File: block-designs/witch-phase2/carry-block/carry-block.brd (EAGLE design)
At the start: 27.9 x 27.9 mm, 11 parts, among them IC1 741G175, IC2 74AHC1G32DBV, IC3 74LS195D, IC4 74AHC1G86DBV

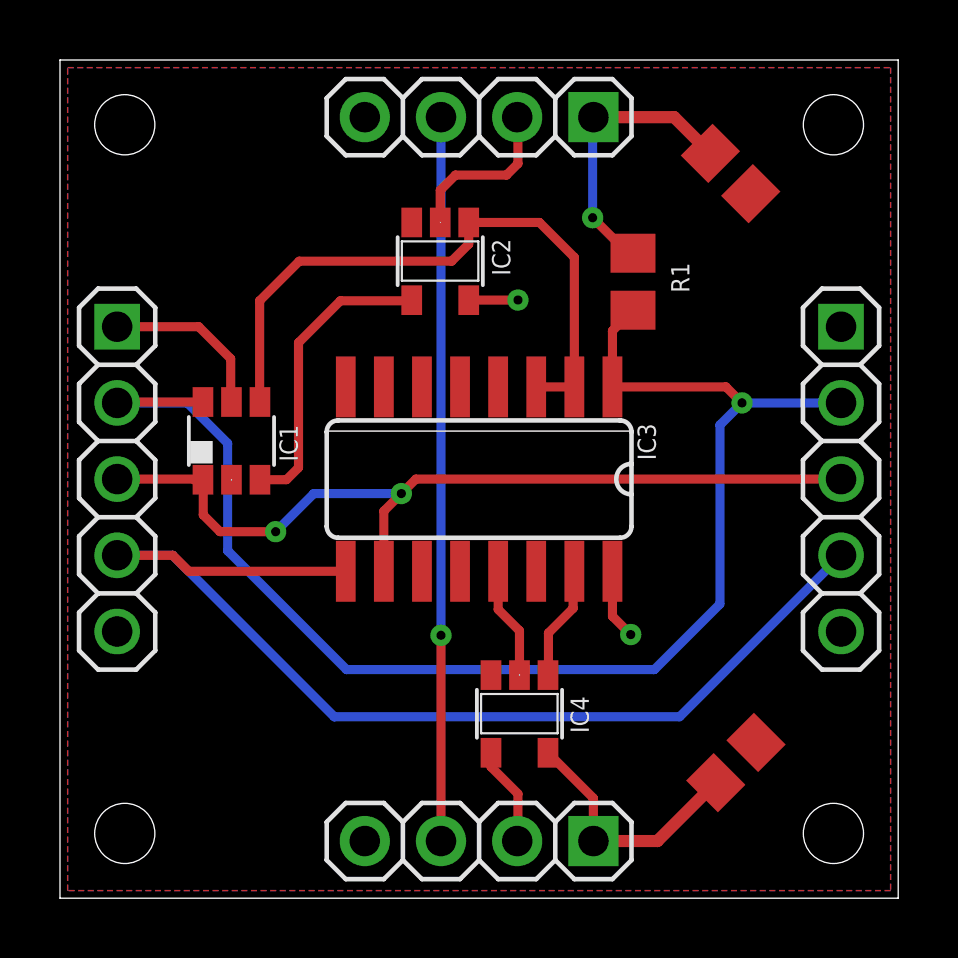
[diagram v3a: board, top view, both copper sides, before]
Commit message: replace or with d-flipflop to fix zc start issue
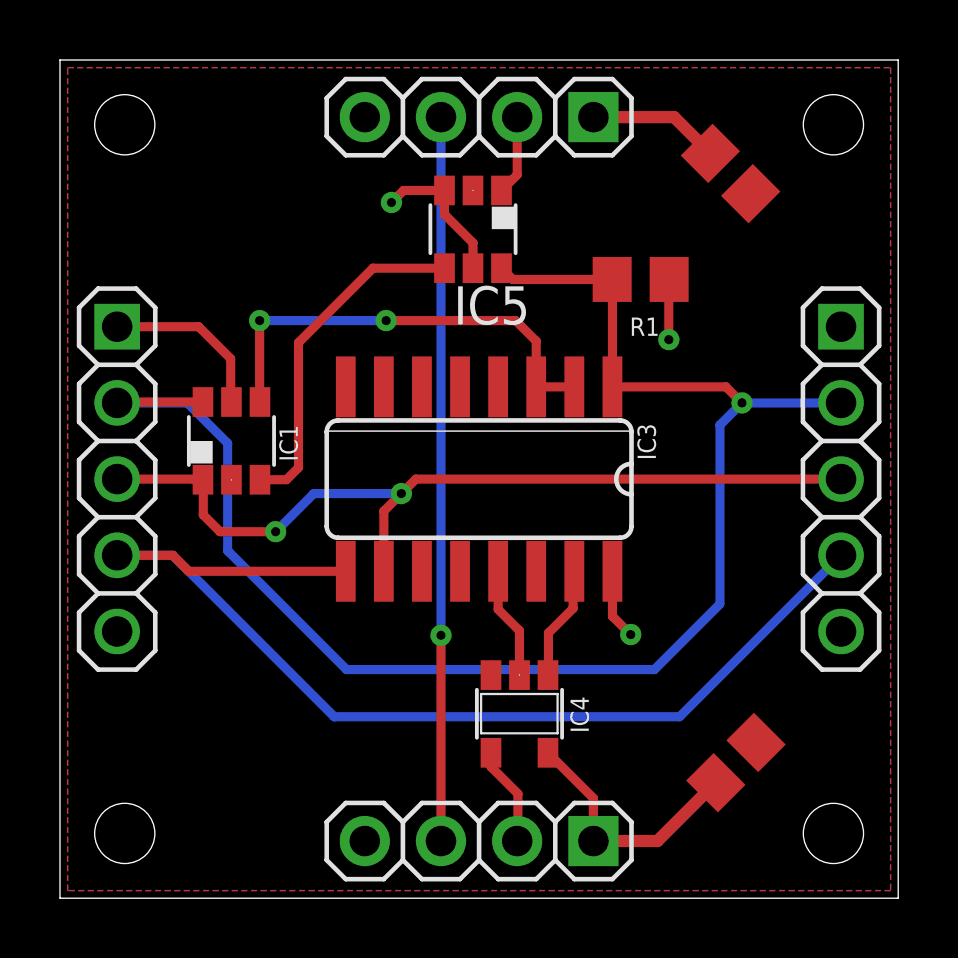
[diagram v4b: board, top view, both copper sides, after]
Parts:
- removed IC2: 74AHC1G32DBV, 74xx-little-us:SOT23-5
- added IC5: 741G175, 74xx-little-us:DBV_R-PDSO-G6
- moved R1 0.27 mm to (19.4, 20.6), turned to 180 degrees
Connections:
- net !RST: now also IC5.6
- net GND: now also IC5.2; no longer IC2.3
- net N$5: now also IC5.4; no longer IC2.4
- net VCC: now also IC5.3, IC5.5; no longer IC2.5
- net ZC: now also IC5.1; no longer IC2.2
- net ZC-OUT: no longer IC2.1
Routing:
- net ZC-OUT: track 21.5 -> 15.1 mm, vias 0 -> 2
- net !RST: track 47.3 -> 51.9 mm
- net ZC: track 5.59 -> 2.66 mm
- net N$5: track 9.98 -> 11.5 mm
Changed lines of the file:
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@@
 <?xml version="1.0" encoding="utf-8"?>
 <!DOCTYPE eagle SYSTEM "eagle.dtd">
-<eagle version="7.3.0">
+<eagle version="7.6.0">
 <drawing>
 <settings>
@@
 <attribute name="VALUE" x="22.86" y="17.78" size="1.27" layer="27" rot="R270"/>
 </element>
-<element name="IC2" library="74xx-little-us" package="SOT23-5" value="74AHC1G32DBV" x="12.6746" y="21.2344" smashed="yes" rot="R180">
-<attribute name="NAME" x="15.0114" y="20.7518" size="0.6096" layer="25" rot="R90"/>
-<attribute name="VALUE" x="15.9766" y="21.5646" size="0.6096" layer="27" rot="R180"/>
-</element>
-<element name="R1" library="resistor" package="R0805" value="" x="19.1008" y="20.5486" smashed="yes" rot="R270">
-<attribute name="NAME" x="20.3708" y="21.1836" size="0.6096" layer="25" rot="R270"/>
-<attribute name="VALUE" x="16.5608" y="21.1836" size="1.27" layer="27" rot="R270"/>
+<element name="R1" library="resistor" package="R0805" value="" x="19.3548" y="20.6248" smashed="yes" rot="R180">
+<attribute name="NAME" x="19.9898" y="19.3548" size="0.6096" layer="25" rot="R180"/>
+<attribute name="VALUE" x="19.9898" y="23.1648" size="1.27" layer="27" rot="R180"/>
 </element>
 <element name="IC1" library="74xx-little-us" package="DBV_R-PDSO-G6" value="741G175" x="5.715" y="15.24" smashed="yes">
@@
 <attribute name="NAME" x="19.2532" y="15.8242" size="0.6096" layer="25" ratio="10" rot="R270"/>
 </element>
+<element name="IC5" library="74xx-little-us" package="DBV_R-PDSO-G6" value="741G175" x="13.7668" y="22.3012" rot="R180"/>
 </elements>
 <signals>
@@
 <vertex x="27.686" y="27.686"/>
 </polygon>
-<contactref element="IC2" pad="3"/>
 <contactref element="IC1" pad="2"/>
 <contactref element="JP2" pad="5"/>
@@
 <contactref element="IC3" pad="5"/>
 <contactref element="IC3" pad="6"/>
+<contactref element="IC5" pad="2"/>
 </signal>
 <signal name="VCC">
@@
 <contactref element="JP4" pad="1"/>
 <contactref element="JP2" pad="1"/>
-<contactref element="IC2" pad="5"/>
 <contactref element="R1" pad="1"/>
 <contactref element="IC1" pad="5"/>
@@
 <wire x1="16.2662" y1="4.8468" x2="17.78" y2="3.333" width="0.3048" layer="1"/>
 <wire x1="17.78" y1="3.333" x2="17.78" y2="1.905" width="0.3048" layer="1"/>
-<wire x1="13.6246" y1="19.9344" x2="13.6292" y2="19.939" width="0.3048" layer="1"/>
-<wire x1="13.6292" y1="19.939" x2="15.2654" y2="19.939" width="0.3048" layer="1"/>
-<via x="15.2654" y="19.939" extent="1-16" drill="0.3048"/>
+<via x="11.049" y="23.1902" extent="1-16" drill="0.3048"/>
 <wire x1="4.6228" y1="19.05" x2="5.6896" y2="17.9832" width="0.3048" layer="1"/>
 <wire x1="5.6896" y1="17.9832" x2="5.6896" y2="16.5654" width="0.3048" layer="1"/>
 <wire x1="5.6896" y1="16.5654" x2="5.715" y2="16.54" width="0.3048" layer="1"/>
-<wire x1="19.1008" y1="21.4986" x2="18.9382" y2="21.4986" width="0.3048" layer="1"/>
-<wire x1="18.9382" y1="21.4986" x2="17.7546" y2="22.6822" width="0.3048" layer="1"/>
-<via x="17.7546" y="22.6822" extent="1-16" drill="0.3048"/>
-<wire x1="17.7546" y1="22.6822" x2="17.7546" y2="26.0096" width="0.3048" layer="16"/>
+<via x="20.2946" y="18.6182" extent="1-16" drill="0.3048"/>
 <wire x1="17.7546" y1="26.0096" x2="17.78" y2="26.035" width="0.3048" layer="16"/>
 <wire x1="17.78" y1="26.035" x2="20.472396875" y2="26.035" width="0.4064" layer="1"/>
@@
 <wire x1="21.858046875" y1="3.849446875" x2="19.9136" y2="1.905" width="0.4064" layer="1"/>
 <wire x1="19.9136" y1="1.905" x2="17.78" y2="1.905" width="0.4064" layer="1"/>
+<contactref element="IC5" pad="5"/>
+<contactref element="IC5" pad="3"/>
+<wire x1="20.3048" y1="20.6248" x2="20.2946" y2="20.6146" width="0.3048" layer="1"/>
+<wire x1="20.2946" y1="20.6146" x2="20.2946" y2="18.6182" width="0.3048" layer="1"/>
+<wire x1="12.8168" y1="23.5912" x2="11.45" y2="23.5912" width="0.3048" layer="1"/>
+<wire x1="11.45" y1="23.5912" x2="11.049" y2="23.1902" width="0.3048" layer="1"/>
+<wire x1="12.8168" y1="23.5912" x2="12.8168" y2="22.794" width="0.3048" layer="1"/>
+<wire x1="12.8168" y1="22.794" x2="13.7668" y2="21.844" width="0.3048" layer="1"/>
+<wire x1="13.7668" y1="21.844" x2="13.7668" y2="21.0012" width="0.3048" layer="1"/>
 </signal>
 <signal name="ZC">
 <contactref element="JP1" pad="2"/>
-<contactref element="IC2" pad="2"/>
-<wire x1="12.6746" y1="22.5244" x2="12.6746" y2="23.5966" width="0.3048" layer="1"/>
-<wire x1="12.6746" y1="23.5966" x2="13.1826" y2="24.1046" width="0.3048" layer="1"/>
-<wire x1="13.1826" y1="24.1046" x2="14.8844" y2="24.1046" width="0.3048" layer="1"/>
-<wire x1="14.8844" y1="24.1046" x2="15.2654" y2="24.4856" width="0.3048" layer="1"/>
-<wire x1="15.2654" y1="24.4856" x2="15.2654" y2="26.0096" width="0.3048" layer="1"/>
-<wire x1="15.2654" y1="26.0096" x2="15.24" y2="26.035" width="0.3048" layer="1"/>
+<contactref element="IC5" pad="1"/>
+<wire x1="14.7168" y1="23.5912" x2="15.24" y2="24.1144" width="0.3048" layer="1"/>
+<wire x1="15.24" y1="24.1144" x2="15.24" y2="26.035" width="0.3048" layer="1"/>
 </signal>
 <signal name="CLK_OUT">
@@
 </signal>
 <signal name="ZC-OUT">
-<contactref element="IC2" pad="1"/>
 <contactref element="IC1" pad="4"/>
 <contactref element="IC3" pad="3"/>
@@
 <wire x1="15.875" y1="17.0434" x2="17.145" y2="17.0434" width="0.3048" layer="1"/>
 <wire x1="17.1196" y1="17.0688" x2="17.145" y2="17.0434" width="0.3048" layer="1"/>
-<wire x1="13.6398" y1="22.5396" x2="13.6246" y2="22.5244" width="0.3048" layer="1"/>
-<wire x1="13.6246" y1="22.5244" x2="15.982" y2="22.5244" width="0.3048" layer="1"/>
-<wire x1="15.982" y1="22.5244" x2="17.145" y2="21.3614" width="0.3048" layer="1"/>
-<wire x1="17.145" y1="21.3614" x2="17.145" y2="17.0434" width="0.3048" layer="1"/>
-<wire x1="13.0556" y1="21.2344" x2="13.6246" y2="21.8034" width="0.3048" layer="1"/>
-<wire x1="13.6246" y1="21.8034" x2="13.6246" y2="22.5244" width="0.3048" layer="1"/>
-<wire x1="13.0556" y1="21.2344" x2="7.9756" y2="21.2344" width="0.3048" layer="1"/>
-<wire x1="7.9756" y1="21.2344" x2="6.6548" y2="19.9136" width="0.3048" layer="1"/>
-<wire x1="6.6548" y1="19.9136" x2="6.6548" y2="16.5502" width="0.3048" layer="1"/>
 <wire x1="6.6548" y1="16.5502" x2="6.665" y2="16.54" width="0.3048" layer="1"/>
+<via x="6.6548" y="19.2532" extent="1-16" drill="0.3048"/>
+<wire x1="6.6548" y1="19.2532" x2="10.8712" y2="19.2532" width="0.3048" layer="16"/>
+<via x="10.8712" y="19.2532" extent="1-16" drill="0.3048"/>
+<wire x1="10.8712" y1="19.2532" x2="15.1892" y2="19.2532" width="0.3048" layer="1"/>
+<wire x1="15.1892" y1="19.2532" x2="15.875" y2="18.5674" width="0.3048" layer="1"/>
+<wire x1="15.875" y1="18.5674" x2="15.875" y2="17.0434" width="0.3048" layer="1"/>
+<wire x1="6.6548" y1="16.5502" x2="6.6548" y2="19.2532" width="0.3048" layer="1"/>
 </signal>
 <signal name="N$5">
-<contactref element="IC2" pad="4"/>
 <contactref element="IC1" pad="3"/>
 <wire x1="7.9502" y1="14.351" x2="7.5492" y2="13.95" width="0.3048" layer="1"/>
 <wire x1="7.9502" y1="14.351" x2="7.9502" y2="18.5166" width="0.3048" layer="1"/>
-<wire x1="7.9502" y1="18.5166" x2="9.3472" y2="19.9136" width="0.3048" layer="1"/>
-<wire x1="9.3472" y1="19.9136" x2="11.7038" y2="19.9136" width="0.3048" layer="1"/>
-<wire x1="11.7038" y1="19.9136" x2="11.7246" y2="19.9344" width="0.3048" layer="1"/>
 <wire x1="7.5492" y1="13.95" x2="6.665" y2="13.95" width="0.3048" layer="1"/>
+<contactref element="IC5" pad="4"/>
+<wire x1="7.9502" y1="18.5166" x2="10.4348" y2="21.0012" width="0.3048" layer="1"/>
+<wire x1="10.4348" y1="21.0012" x2="12.8168" y2="21.0012" width="0.3048" layer="1"/>
 </signal>
 <signal name="!MCLK">
@@
 <wire x1="4.765" y1="16.54" x2="1.935" y2="16.54" width="0.3048" layer="1"/>
 <wire x1="1.935" y1="16.54" x2="1.905" y2="16.51" width="0.3048" layer="1"/>
-<wire x1="18.415" y1="17.0434" x2="18.415" y2="18.9128" width="0.3048" layer="1"/>
-<wire x1="18.415" y1="18.9128" x2="19.1008" y2="19.5986" width="0.3048" layer="1"/>
+<contactref element="IC5" pad="6"/>
+<wire x1="14.7168" y1="21.0012" x2="15.0932" y2="20.6248" width="0.3048" layer="1"/>
+<wire x1="15.0932" y1="20.6248" x2="18.4048" y2="20.6248" width="0.3048" layer="1"/>
+<wire x1="18.4048" y1="20.6248" x2="18.415" y2="20.6146" width="0.3048" layer="1"/>
+<wire x1="18.415" y1="20.6146" x2="18.415" y2="17.0434" width="0.3048" layer="1"/>
 </signal>
 <signal name="CARRY_EN">
